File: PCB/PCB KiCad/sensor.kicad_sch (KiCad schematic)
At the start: 12 parts, among them U1 OPA2376AID

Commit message: Minor schematic cleanup!
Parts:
- D1: footprint Diode_THT:D_A-405_P2.54mm_Vertical_KathodeUp -> Diode_SMD:D_1206_3216Metric_Pad1.42x1.75mm_HandSolder
- gave numbers to parts that had none: 1
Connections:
- net +3V3 renamed +3.3V
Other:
- moved on the sheet: C1, C2, C3, C4, C5, D1, J1, R1, R2, R3, R4, U1

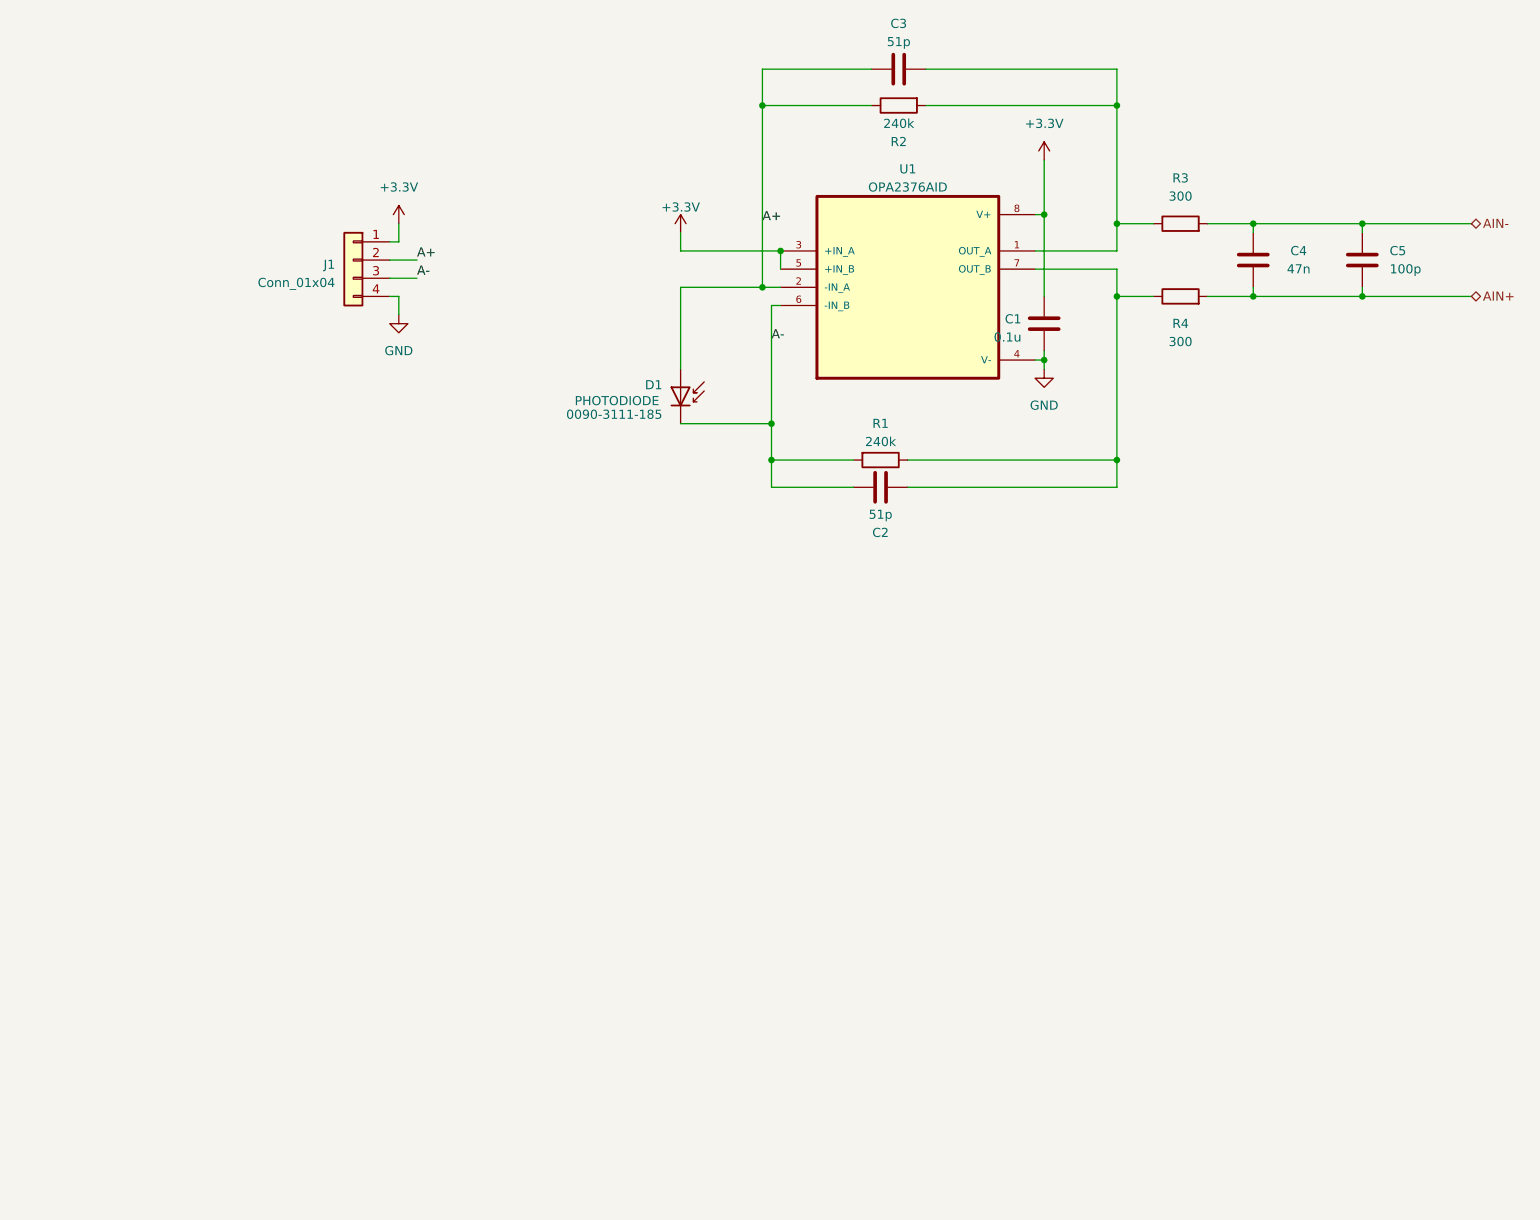
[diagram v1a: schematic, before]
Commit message: Giant schematic cleanup to make more sense of the sensor circuit and just clean everything up a bit.
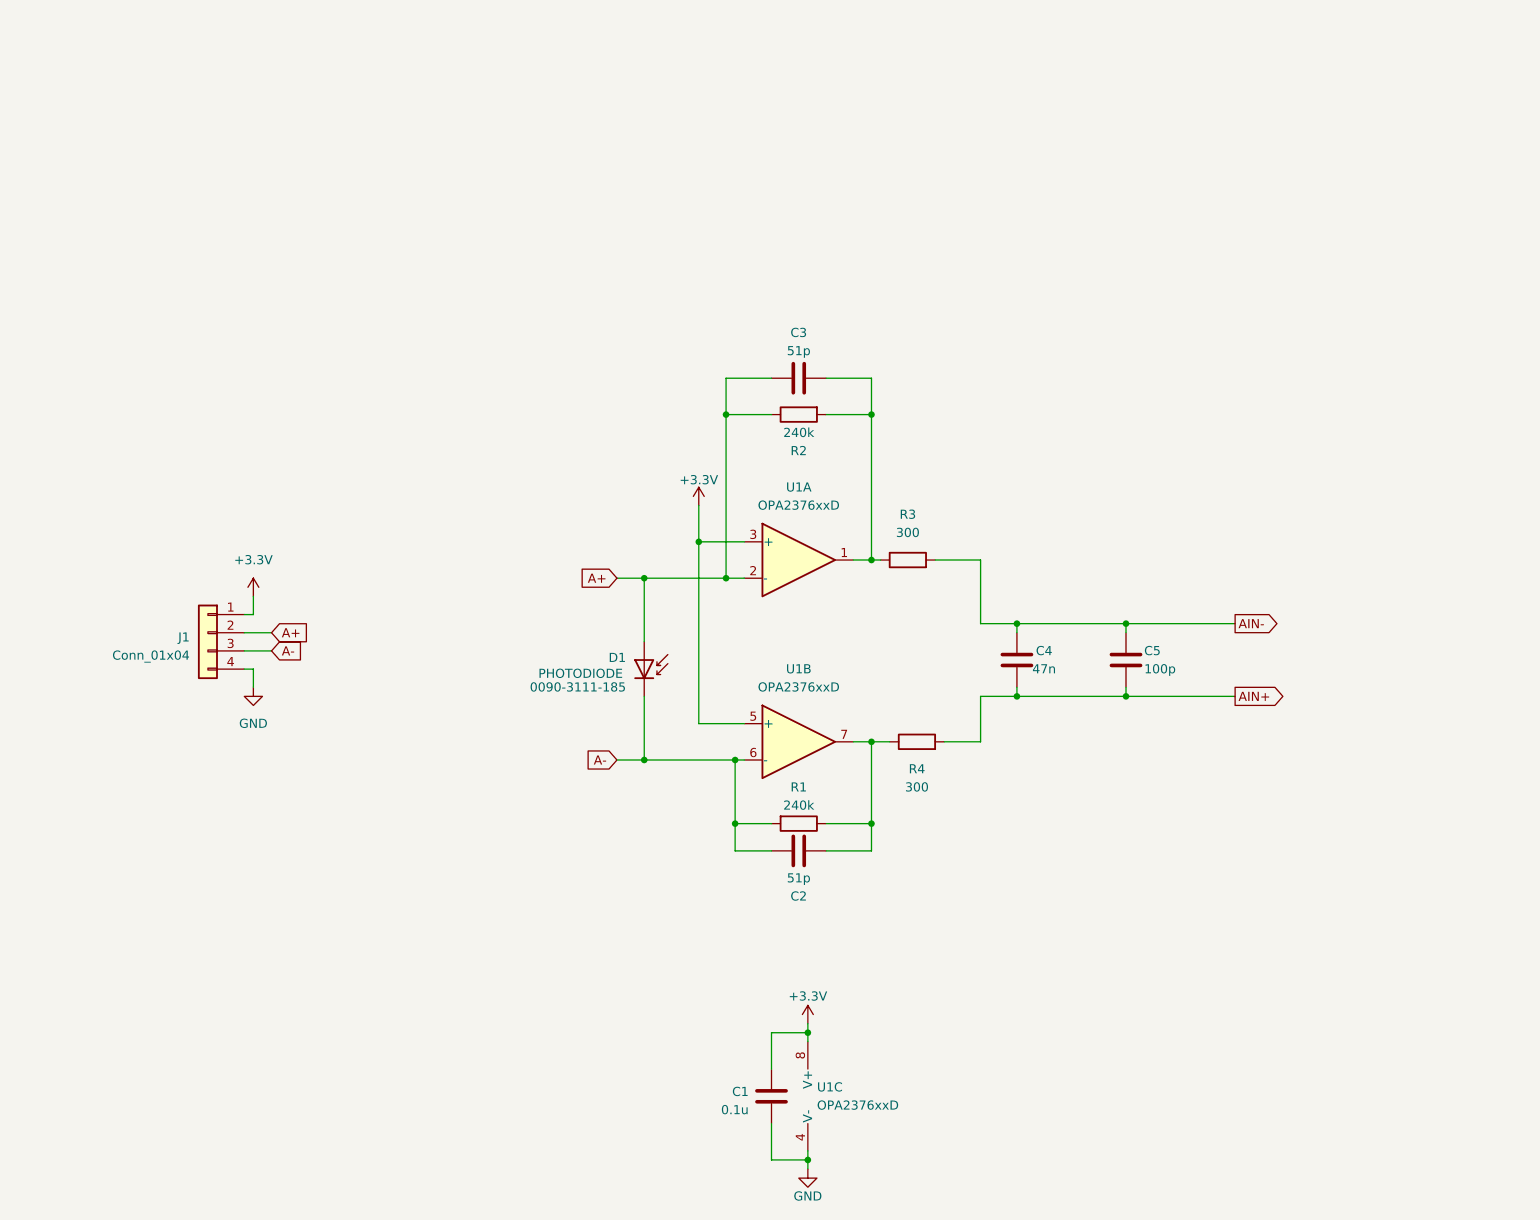
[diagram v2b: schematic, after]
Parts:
- removed U1: OPA2376AID, OPA2376AID:SOIC127P599X175-8N, symbol OPA2376AID:OPA2376AID
- added U1: OPA2376xxD, OPA2376AID:SOIC127P599X175-8N, symbol Amplifier_Operational:OPA2376xxD
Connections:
- net +3.3V: now also U1.3 (+), U1.5 (+), U1.8 (V+)
- net A+: now also U1.2 (-)
- net A-: now also U1.6 (-)
- net GND: now also U1.4 (V-)
- net at C2.2, R1.1, R4.1: now also U1.7
- net at C3.2, R2.2, R3.1: now also U1.1
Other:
- moved on the sheet: C1, C2, C3, C4, C5, D1, J1, R1, R2, R3, R4
